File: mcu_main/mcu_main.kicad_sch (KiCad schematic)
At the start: 18 parts, among them J2 Conn_01x10_Pin, J3 Conn_01x06_Pin, SW1 SW_Push_Dual, SW2 SW_Push_Dual, U1 ESP32-S3-WROOM-1, U3 SGM2212-3.3

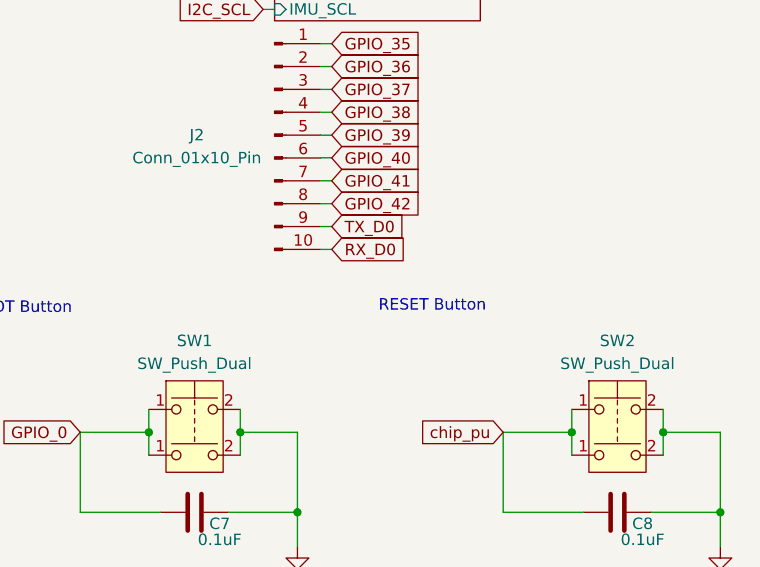
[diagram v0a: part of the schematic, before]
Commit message: fixed the power section of the pcb layout
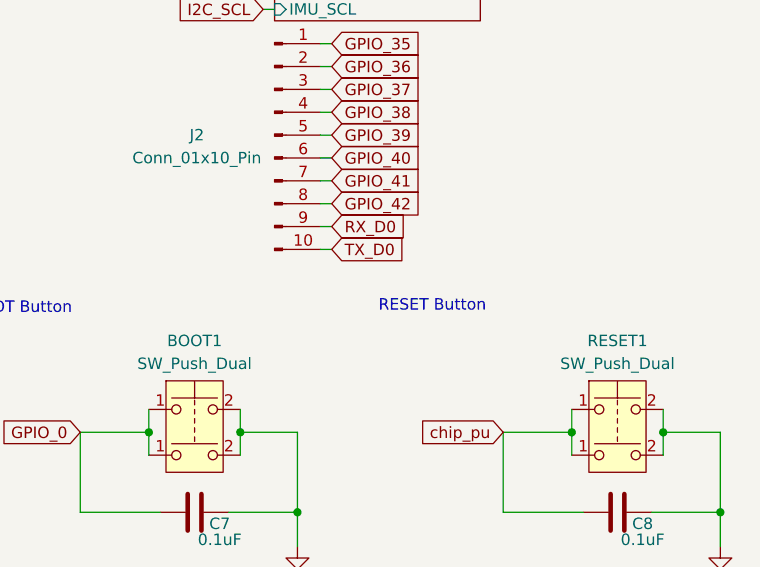
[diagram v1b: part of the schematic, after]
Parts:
- renumbered SW1 to BOOT1, SW2 to RESET1
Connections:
- net RX_D0: now also J2.9 (Pin_9); no longer J2.10 (Pin_10)
- net TX_D0: now also J2.10 (Pin_10); no longer J2.9 (Pin_9)
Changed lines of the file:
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@@
 	(wire
 		(pts
-			(xy 236.22 166.37) (xy 234.95 166.37)
-		)
-		(stroke
-			(width 0)
-			(type default)
-		)
-	)
-	(wire
-		(pts
 			(xy 208.28 189.23) (xy 215.9 189.23)
 		)
@@
 	(wire
 		(pts
+			(xy 236.22 168.91) (xy 234.95 168.91)
+		)
+		(stroke
+			(width 0)
+			(type default)
+		)
+	)
+	(wire
+		(pts
 			(xy 255.27 189.23) (xy 262.89 189.23)
 		)
@@
 	(wire
 		(pts
+			(xy 236.22 166.37) (xy 234.95 166.37)
+		)
+		(stroke
+			(width 0)
+			(type default)
+		)
+	)
+	(wire
+		(pts
 			(xy 255.27 198.12) (xy 255.27 189.23)
 		)
@@
 	(wire
 		(pts
-			(xy 236.22 168.91) (xy 234.95 168.91)
-		)
-		(stroke
-			(width 0)
-			(type default)
-		)
-	)
-	(wire
-		(pts
 			(xy 279.4 189.23) (xy 273.05 189.23)
 		)
@@
 	(global_label "TX_D0"
 		(shape input)
-		(at 236.22 166.37 0)
+		(at 236.22 168.91 0)
 		(fields_autoplaced yes)
 		(effects
@@
 		)
 		(property "Intersheetrefs" "${INTERSHEET_REFS}"
-			(at 244.8294 166.37 0)
+			(at 244.8294 168.91 0)
 			(effects
 				(font
@@
 	(global_label "RX_D0"
 		(shape input)
-		(at 236.22 168.91 0)
+		(at 236.22 166.37 0)
 		(fields_autoplaced yes)
 		(effects
@@
 		)
 		(property "Intersheetrefs" "${INTERSHEET_REFS}"
-			(at 245.1318 168.91 0)
+			(at 245.1318 166.37 0)
 			(effects
 				(font
@@
 		(polyline
 			(pts
-				(xy 134.6351 119.3433) (xy 118.1251 119.3433) (xy 118.1268 106.7591) (xy 134.6368 106.7591)
+				(xy 58.42 161.29) (xy 58.42 209.55) (xy 139.7 209.55) (xy 139.7 161.29)
 			)
 			(stroke
@@
 		(polyline
 			(pts
-				(xy 241.3 176.53) (xy 241.3 209.55) (xy 285.75 209.55) (xy 285.75 176.53)
+				(xy 129.1488 40.6278) (xy 129.1489 71.1078) (xy 147.32 71.1199) (xy 147.3199 40.6399)
 			)
 			(stroke
@@
 		(polyline
 			(pts
-				(xy 58.42 161.29) (xy 58.42 209.55) (xy 139.7 209.55) (xy 139.7 161.29)
+				(xy 213.676 127.0197) (xy 200.66 127) (xy 200.6533 119.1467) (xy 213.6693 119.1664)
 			)
 			(stroke
@@
 		(polyline
 			(pts
-				(xy 129.1488 40.6278) (xy 129.1489 71.1078) (xy 147.32 71.1199) (xy 147.3199 40.6399)
+				(xy 195.58 176.53) (xy 195.58 209.55) (xy 238.76 209.55) (xy 238.76 176.53)
 			)
 			(stroke
@@
 		(polyline
 			(pts
-				(xy 213.676 127.0197) (xy 200.66 127) (xy 200.6533 119.1467) (xy 213.6693 119.1664)
+				(xy 241.3 176.53) (xy 241.3 209.55) (xy 285.75 209.55) (xy 285.75 176.53)
 			)
 			(stroke
@@
 		(polyline
 			(pts
-				(xy 195.58 176.53) (xy 195.58 209.55) (xy 238.76 209.55) (xy 238.76 176.53)
+				(xy 134.6351 119.3433) (xy 118.1251 119.3433) (xy 118.1268 106.7591) (xy 134.6368 106.7591)
 			)
 			(stroke
@@
 		(on_board yes)
 		(dnp no)
-		(property "Reference" "SW1"
+		(property "Reference" "BOOT1"
 			(at 220.98 179.07 0)
 			(effects
@@
 			(project "mcu_main"
 				(path "/8c1e5247-e001-4f3c-b236-a22b9c821843"
-					(reference "SW1")
+					(reference "BOOT1")
 					(unit 1)
 				)
@@
 		(on_board yes)
 		(dnp no)
-		(property "Reference" "SW2"
+		(property "Reference" "RESET1"
 			(at 267.97 179.07 0)
 			(effects
@@
 			(project "mcu_main"
 				(path "/8c1e5247-e001-4f3c-b236-a22b9c821843"
-					(reference "SW2")
+					(reference "RESET1")
 					(unit 1)
 				)

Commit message: added most things to the pcb, review required
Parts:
- added J10: Conn_01x02_Pin, Connector_PinHeader_2.54mm:PinHeader_1x02_P2.54mm_Vertical, symbol Connector:Conn_01x02_Pin
- J2: footprint Connector_Molex:Molex_KK-254_AE-6410-10A_1x10_P2.54mm_Vertical -> Connector_PinHeader_2.54mm:PinHeader_1x10_P2.54mm_Vertical
- J3: footprint Connector_Molex:Molex_KK-254_AE-6410-06A_1x06_P2.54mm_Vertical -> Connector_PinHeader_2.54mm:PinHeader_1x06_P2.54mm_Vertical
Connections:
- net Display_CS is gone; now on net Display_LED: U1.22 (IO14)
- net Time of flight sensor/TOF_XSHUT is gone; now on net Time of flight sensor/TOF_GPIO1: U1.26 (IO45)
- net +5V: now also J10.1 (Pin_1)
- net Display_DC/RS: now also U1.17 (IO9); no longer U1.12 (IO8)
- net Display_LED: no longer U1.17 (IO9)
- net Display_RST: now also U1.16 (IO46); no longer U1.7 (IO7)
- net GND: now also J10.2 (Pin_2)
- net GPIO_15: now also J3.2 (Pin_2); no longer J3.1 (Pin_1)
- net GPIO_16: now also J3.3 (Pin_3); no longer J3.2 (Pin_2)
- net GPIO_17: now also J3.4 (Pin_4); no longer J3.3 (Pin_3)
- net GPIO_18: now also J3.5 (Pin_5); no longer J3.4 (Pin_4)
- net Time of flight sensor/TOF_GPIO1: no longer U1.16 (IO46)
- net GPIO_21 renamed GPIO_8
- net GPIO_8: now also U1.12 (IO8); no longer U1.23 (IO21)
- net GPIO_3 renamed sdcard_CS
- net sdcard_CS: no longer J3.5 (Pin_5)
- new net GPIO_7: J3.1 (Pin_1), U1.7 (IO7)
- new net TOF_XSHUT: U1.23 (IO21)

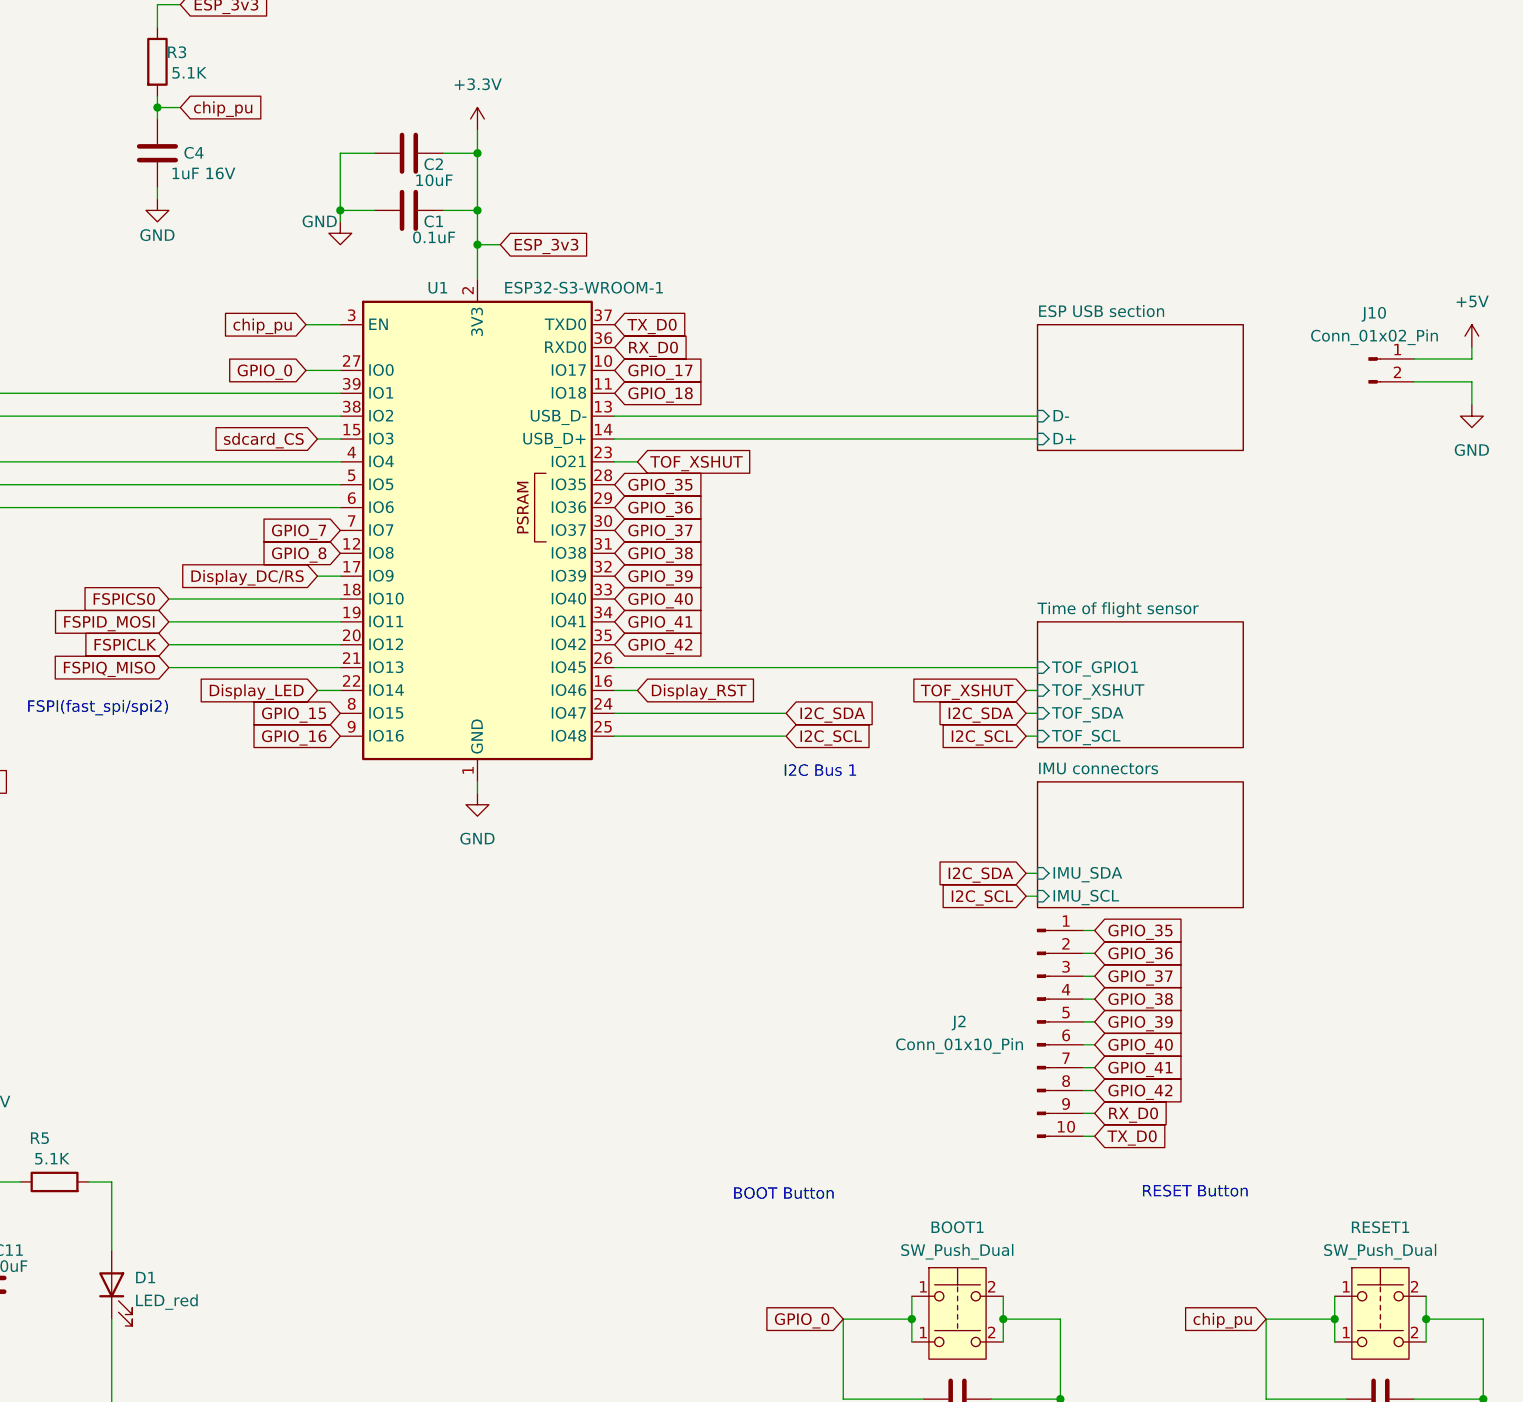
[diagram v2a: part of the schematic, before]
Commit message: Fixed most drc violations
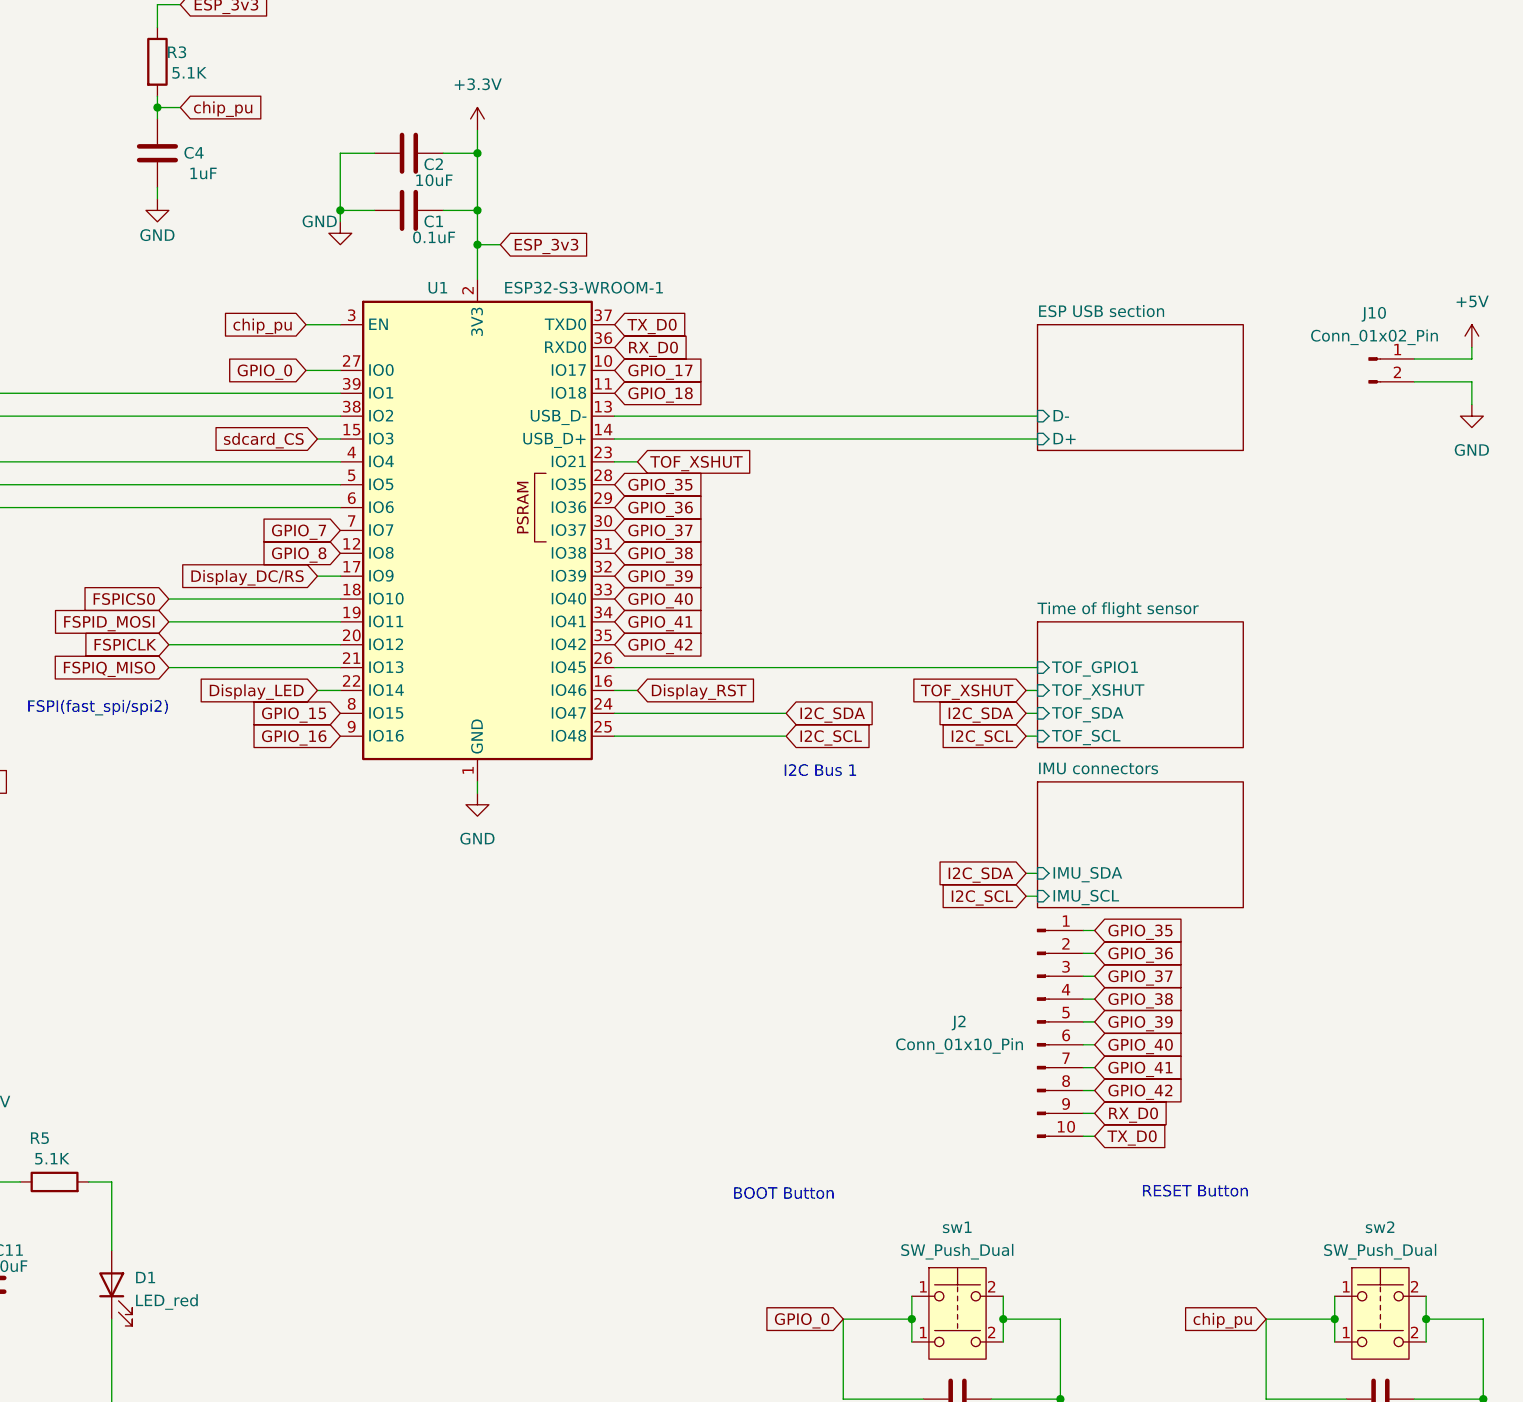
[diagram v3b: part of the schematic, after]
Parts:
- C4: value 1uF 16V -> 1uF
- renumbered BOOT1 to sw1, RESET1 to sw2
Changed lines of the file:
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@@
+		(polyline
+			(pts
+				(xy 195.58 176.53) (xy 195.58 209.55) (xy 238.76 209.55) (xy 238.76 176.53)
+			)
+			(stroke
+				(width 0)
+				(type dash)
+			)
+			(fill
+				(type none)
+			)
+		)
+	)
+	(rule_area
+		(polyline
+			(pts
+				(xy 213.676 127.0197) (xy 200.66 127) (xy 200.6533 119.1467) (xy 213.6693 119.1664)
+			)
+			(stroke
+				(width 0)
+				(type dash)
+			)
+			(fill
+				(type none)
+			)
+		)
+	)
+	(rule_area
 		(polyline
 			(pts
 				(xy 58.42 161.29) (xy 58.42 209.55) (xy 139.7 209.55) (xy 139.7 161.29)
+			)
+			(stroke
+				(width 0)
+				(type dash)
+			)
+			(fill
+				(type none)
+			)
+		)
+	)
+	(rule_area
+		(polyline
+			(pts
+				(xy 241.3 176.53) (xy 241.3 209.55) (xy 285.75 209.55) (xy 285.75 176.53)
+			)
+			(stroke
+				(width 0)
+				(type dash)
+			)
+			(fill
+				(type none)
+			)
+		)
+	)
+	(rule_area
+		(polyline
+			(pts
+				(xy 129.1488 40.6278) (xy 129.1489 71.1078) (xy 147.32 71.1199) (xy 147.3199 40.6399)
 			)
 			(stroke
@@
 		)
 	)
-	(rule_area
-		(polyline
-			(pts
-				(xy 213.676 127.0197) (xy 200.66 127) (xy 200.6533 119.1467) (xy 213.6693 119.1664)
-			)
-			(stroke
-				(width 0)
-				(type dash)
-			)
-			(fill
-				(type none)
-			)
-		)
-	)
-	(rule_area
-		(polyline
-			(pts
-				(xy 129.1488 40.6278) (xy 129.1489 71.1078) (xy 147.32 71.1199) (xy 147.3199 40.6399)
-			)
-			(stroke
-				(width 0)
-				(type dash)
-			)
-			(fill
-				(type none)
-			)
-		)
-	)
-	(rule_area
-		(polyline
-			(pts
-				(xy 195.58 176.53) (xy 195.58 209.55) (xy 238.76 209.55) (xy 238.76 176.53)
-			)
-			(stroke
-				(width 0)
-				(type dash)
-			)
-			(fill
-				(type none)
-			)
-		)
-	)
-	(rule_area
-		(polyline
-			(pts
-				(xy 241.3 176.53) (xy 241.3 209.55) (xy 285.75 209.55) (xy 285.75 176.53)
-			)
-			(stroke
-				(width 0)
-				(type dash)
-			)
-			(fill
-				(type none)
-			)
-		)
-	)
 	(symbol
 		(lib_id "Connector:Conn_01x06_Pin")
@@
 		(on_board yes)
 		(dnp no)
-		(property "Reference" "BOOT1"
+		(property "Reference" "sw1"
 			(at 220.98 179.07 0)
 			(effects
@@
 			(project "mcu_main"
 				(path "/8c1e5247-e001-4f3c-b236-a22b9c821843"
-					(reference "BOOT1")
+					(reference "sw1")
 					(unit 1)
 				)
@@
 			)
 		)
-		(property "Value" "1uF 16V"
+		(property "Value" "1uF"
 			(at 137.16 61.976 0)
 			(effects
@@
 		(on_board yes)
 		(dnp no)
-		(property "Reference" "RESET1"
+		(property "Reference" "sw2"
 			(at 267.97 179.07 0)
 			(effects
@@
 			(project "mcu_main"
 				(path "/8c1e5247-e001-4f3c-b236-a22b9c821843"
-					(reference "RESET1")
-					(unit 1)
-				)
+					(reference "sw2")
+					(unit 1)
+				)
